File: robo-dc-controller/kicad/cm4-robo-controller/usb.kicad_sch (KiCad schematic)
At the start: 35 parts, among them U2 TPD4EUSB30DQAR-N, U3 FSUSB42MUX, U4 USB2514B-I/M2, U5 AP22653W6-7, U6 TPD4EUSB30DQAR-N, X1 X322524MOB4SI

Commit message: Fixing up usb.kicad+sch
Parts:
- removed C10, C6, C7, C8, C9: 100n, Capacitor_SMD:C_0402_1005Metric, symbol Device:C
- added C10, C19, C6, C7, C8, C9: 100nF, PCM_JLCPCB:C_0402, symbol PCM_JLCPCB-Capacitors:0402,100nF
- C3: VOLTAGE RATING (none) -> 10V
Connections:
- net 3V3_CM4: now also C10.1, C19.1, C6.1, C7.1, C8.1, C9.1
- net GND: now also C10.2, C19.2, C6.2, C7.2, C8.2, C9.2
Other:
- note added: "3.3V Caps for U3 and U4 VDD/VCC."
- note added: "4-Port USB Hub (only using 2 ports)"
- note added: "Current-limited high-side switch"
- note added: "Place each 100nF next to its own U4 supply pin (pins 5, 10, 15, 23, 29, 36) One 100nF place near pin 1 of U3"
- note added: "Ports 3 and 4 are unused: pins 6-9 aren't connected. Reset: RESET_N (pin 26) is on nEXTRST, which leaves this sheet."
- note added: "Protects both USB-A ports (4 lines). Diode clamps VBUS. Place both at USB1."
- note added: "Supplies and protects the 5V going out to the USB-A ports ILIM with 15K resistor limits to ~1.75A"
- note added: "USB - 2 Ports"
- note added: "USB-A ESD"
- note added: "USB-C ESD"
- note added: "USB-C Port for CM4 Flashing (rpiboot)"
- note added: "USB_OTG_ID: high = CM4 device mode (rpiboot), low/GND = CM4 host. Needs otg_mode=1 in config.txt."
- note removed: "U21 protects both USB-A ports (4 lines). D36 clamps VBUS. Place both at USB1."
- note removed: "USB"
- title: (none) -> USB
- moved on the sheet: C1, C11, C12, C13, C14, C15, C16, C2, C3, C4, C5, D1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

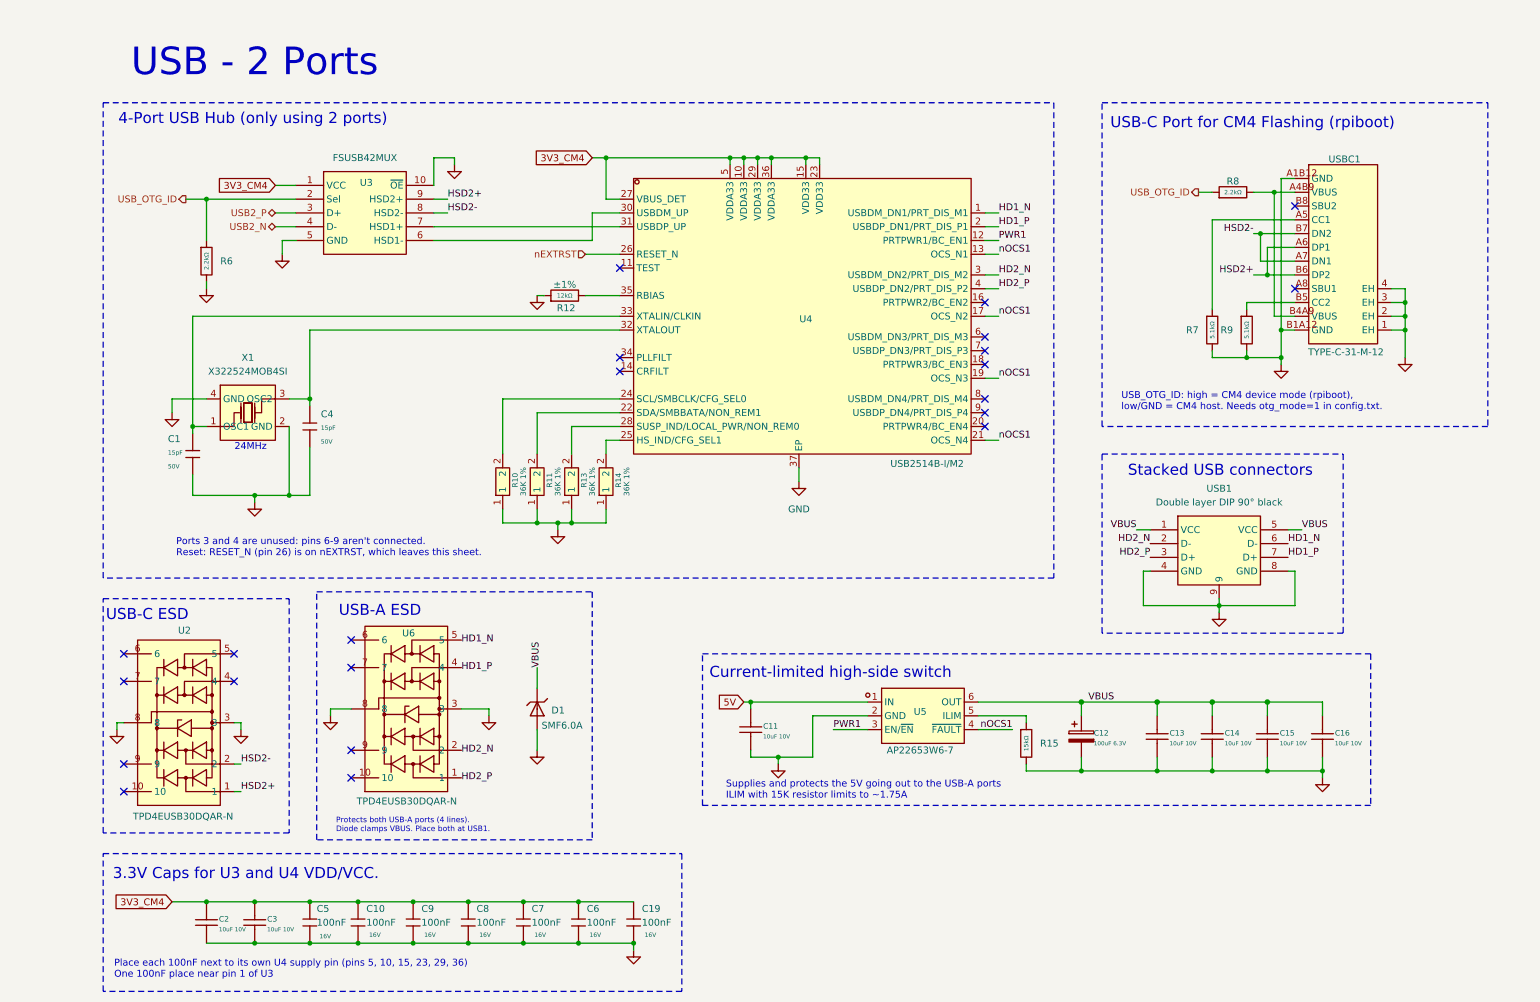
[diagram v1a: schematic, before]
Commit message: USB sheet: add 2-port expansion header, ESD, and design notes
Use all four USB2514B downstream ports: ports 1-2 stay on the USB1
type-A stack, ports 3-4 now go to J14, a 2x5 header with the standard
PC front-panel USB 2.0 pinout. Ports 3 and 4 were previously left
floating, which the Microchip design checklist disallows.

Add U11 (TPD4EUSB30) ESD protection on the expansion pair, D3 (SMF6.0A)
VBUS clamp and C20 local bulk at the header, plus C19 decoupling for
U3 VCC.

Move the 100nF decoupling caps to the JLC basic part (LCSC C1525) so
they are sourced in the assembly BOM, and set J14's pin types to
passive to clear the ERC warnings. ERC on this sheet is now clean.

Document the sheet: purpose of U2/U4/U5/U6, the USB-C device port and
its OTG signalling, the shared ~1.75A port-power budget, and the J14
key-pin assembly note.
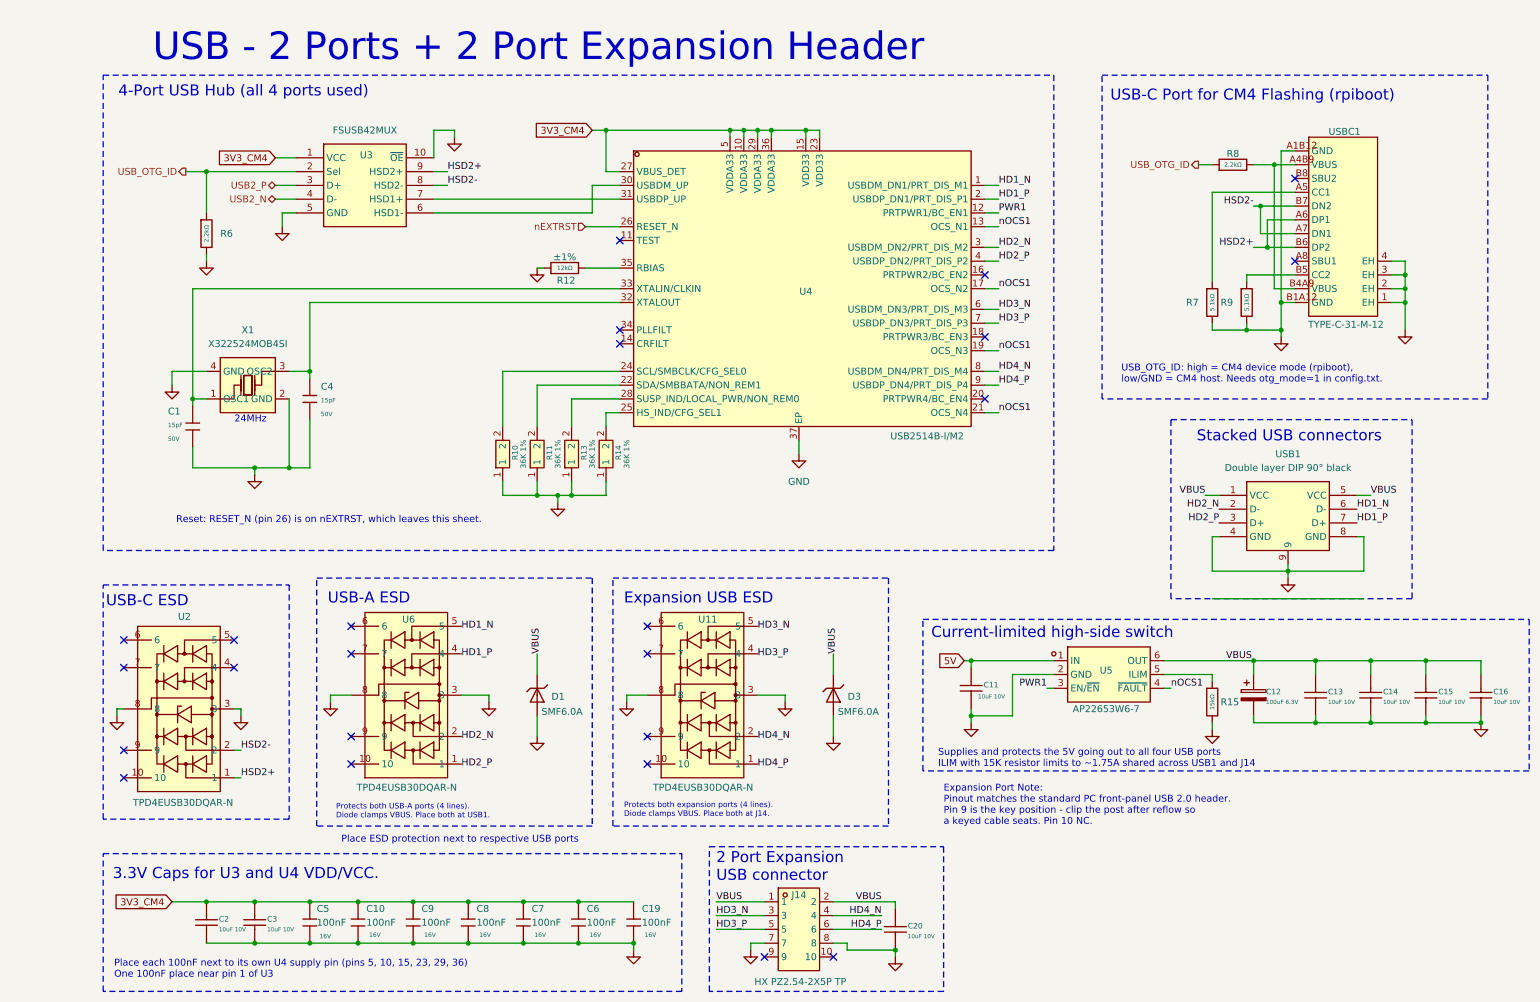
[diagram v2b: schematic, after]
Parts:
- added C20: 10uF 10V, MyParts:C0805, symbol MyParts:CL21B106KPQNNNE
- added D3: SMF6.0A, PCM_JLCPCB:D_SOD-123FL, symbol PCM_JLCPCB-Diodes:TVS-Uni,SMF6.0A
- added J14: HX PZ2.54-2X5P TP, MyParts:HDR-SMD_10P-P2.54-V-M-R2-C5-LS7.5, symbol MyParts:HXPZ2.54-2X5PTP
- added U11: TPD4EUSB30DQAR-N, MyParts:DFN-10_L2.5-W1.0-P0.50-BL-A, symbol MyParts:TPD4EUSB30DQAR-N
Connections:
- net GND: now also C20.1, D3.2, J14.7, J14.8, U11.3, U11.8
- net VBUS: now also C20.2, D3.1, J14.1, J14.2
- net HD3_N: now reaches U4.6 (USBDM_DN3/PRT_DIS_M3)
- net HD3_N: now also J14.3, U11.5
- net HD3_P: now reaches U4.7 (USBDP_DN3/PRT_DIS_P3)
- net HD3_P: now also J14.5, U11.4
- net HD4_N: now reaches U4.8 (USBDM_DN4/PRT_DIS_M4)
- net HD4_N: now also J14.4, U11.2
- net HD4_P: now reaches U4.9 (USBDP_DN4/PRT_DIS_P4)
- net HD4_P: now also J14.6, U11.1
- no-connect marks 22 -> 24
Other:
- note added: "2 Port Expansion USB connector"
- note added: "4-Port USB Hub (all 4 ports used)"
- note added: "Expansion Port Note: Pinout matches the standard PC front-panel USB 2.0 header. Pin 9 is the key position - clip the post after reflow so a keyed cable seats. Pin 10 NC."
- note added: "Expansion USB ESD"
- note added: "Place ESD protection next to respective USB ports"
- note added: "Protects both expansion ports (4 lines). Diode clamps VBUS. Place both at J14."
- note added: "Reset: RESET_N (pin 26) is on nEXTRST, which leaves this sheet."
- note added: "Supplies and protects the 5V going out to all four USB ports ILIM with 15K resistor limits to ~1.75A shared across USB1 and J14"
- note added: "USB - 2 Ports + 2 Port Expansion Header"
- note removed: "4-Port USB Hub (only using 2 ports)"
- note removed: "Ports 3 and 4 are unused: pins 6-9 aren't connected. Reset: RESET_N (pin 26) is on nEXTRST, which leaves this sheet."
- note removed: "Supplies and protects the 5V going out to the USB-A ports ILIM with 15K resistor limits to ~1.75A"
- note removed: "USB - 2 Ports"
- moved on the sheet: C1, C11, C12, C13, C14, C15, C16, C4, D1, R10, R11, R12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

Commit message: CM4 carrier: GPS sheet integration, U12 expansion header, power fixes
Populate U12 (2x12 expansion header) on the CM4_Connectors sheet:
all 19 CM4 signals plus 3V3_CM4 and four grounds, with 2.2k I2C
pull-ups (R113/R114) on GPIO2/GPIO3. Value matches the CM4IO
reference design, which uses 2.2k on SDA1/SCL1.

Wire the new GPS sheet (MAX-M10S) into the CM4 sheet: add sheet pins
for GPS_RX_MCU, GPS_TX_MCU and 1PPS_MCU. The UART lands on UART3
(GPIO4 = TXD3 to the GPS RXD, GPIO5 = RXD3 from the GPS TXD) and
1PPS on GPIO16. Needs dtoverlay=uart3 in config.txt. The leftover
CM4_TX/CM4_RX/1PPS_MCU hierarchical labels, which pointed at a root
sheet with no matching pins, become local labels on those nets.

Fix the orphaned 3V3 label on the GPS sheet, which left the MS621FE
backup cell with no charge path, and scope 3V3_CM4 to the CM4
hierarchy: local labels in the CM4 sheet, hierarchical labels plus
sheet pins in each consuming sub-sheet. Net membership is unchanged
at 30 nodes.

Add PWR_FLAGs on the 5V rail and on GND. Both are driven through
passive parts (an inductor and ground symbols respectively), so ERC
could not see a driver.

ERC: 55 -> 40 violations. Of the remainder, 30 are the RoboClaw U1,
which is placed on the root sheet but not yet wired.
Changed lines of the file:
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@@
 		)
 	)
-	(global_label "3V3_CM4"
+	(hierarchical_label "3V3_CM4"
 		(shape input)
 		(at 50.8 40.64 180)
-		(fields_autoplaced yes)
 		(effects
 			(font
@@
 			(justify right)
 		)
-		(property "Intersheetrefs" "${INTERSHEET_REFS}"
-			(at 39.4087 40.64 0)
-			(hide yes)
-			(show_name no)
-			(do_not_autoplace no)
-			(effects
-				(font
-					(size 1.27 1.27)
-				)
-				(justify right)
-			)
-		)
 	)
-	(global_label "3V3_CM4"
+	(hierarchical_label "3V3_CM4"
 		(shape input)
 		(at 109.22 35.56 180)
-		(fields_autoplaced yes)
 		(effects
 			(font
@@
 			(justify right)
 		)
-		(property "Intersheetrefs" "${INTERSHEET_REFS}"
-			(at 97.8287 35.56 0)
-			(hide yes)
-			(show_name no)
-			(do_not_autoplace no)
-			(effects
-				(font
-					(size 1.27 1.27)
-				)
-				(justify right)
-			)
-		)
 	)
 	(global_label "5V"
@@
 		)
 	)
-	(global_label "3V3_CM4"
+	(hierarchical_label "3V3_CM4"
 		(shape input)
 		(at 31.75 177.8 180)
-		(fields_autoplaced yes)
 		(effects
 			(font
@@
 			(justify right)
 		)
-		(property "Intersheetrefs" "${INTERSHEET_REFS}"
-			(at 20.3587 177.8 0)
-			(hide yes)
-			(show_name no)
-			(do_not_autoplace no)
-			(effects
-				(font
-					(size 1.27 1.27)
-				)
-				(justify right)
-			)
-		)
 	)
 	(hierarchical_label "USB2_N"
@@
 			)
 		)
-		(property "Description" ""
+		(property "Description" "Power symbol creates a global label with name \"GND\" , ground"
 			(at 165.1 187.96 0)
 			(show_name no)
@@
 			)
 		)
-		(property "Description" ""
+		(property "Description" "Power symbol creates a global label with name \"GND\" , ground"
 			(at 138.43 186.69 0)
 			(show_name no)

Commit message: Updates
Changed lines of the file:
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@@
 	(wire
 		(pts
-			(xy 223.52 121.92) (xy 251.46 121.92)
-		)
-		(stroke
-			(width 0)
-			(type default)
-		)
-	)
-	(wire
-		(pts
 			(xy 57.15 67.31) (xy 114.3 67.31)
 		)
@@
 		)
 	)
-	(hierarchical_label "3V3_CM4"
-		(shape input)
-		(at 50.8 40.64 180)
-		(effects
-			(font
-				(size 1.27 1.27)
-			)
-			(justify right)
-		)
-	)
-	(hierarchical_label "3V3_CM4"
-		(shape input)
-		(at 109.22 35.56 180)
-		(effects
-			(font
-				(size 1.27 1.27)
-			)
-			(justify right)
-		)
-	)
 	(global_label "5V"
 		(shape input)
@@
 		)
 	)
-	(hierarchical_label "3V3_CM4"
-		(shape input)
-		(at 31.75 177.8 180)
-		(effects
-			(font
-				(size 1.27 1.27)
-			)
-			(justify right)
-		)
-	)
 	(hierarchical_label "USB2_N"
 		(shape bidirectional)
@@
 		)
 	)
+	(hierarchical_label "3V3_CM4"
+		(shape input)
+		(at 50.8 40.64 180)
+		(effects
+			(font
+				(size 1.27 1.27)
+			)
+			(justify right)
+		)
+	)
+	(hierarchical_label "3V3_CM4"
+		(shape input)
+		(at 109.22 35.56 180)
+		(effects
+			(font
+				(size 1.27 1.27)
+			)
+			(justify right)
+		)
+	)
 	(hierarchical_label "USB2_P"
 		(shape bidirectional)
@@
 		)
 	)
+	(hierarchical_label "3V3_CM4"
+		(shape input)
+		(at 31.75 177.8 180)
+		(effects
+			(font
+				(size 1.27 1.27)
+			)
+			(justify right)
+		)
+	)
 	(hierarchical_label "nEXTRST"
 		(shape input)
@@
 		(property "Description" "Power symbol creates a global label with name \"GND\" , ground"
 			(at 165.1 187.96 0)
+			(hide yes)
 			(show_name no)
 			(do_not_autoplace no)
@@
 		(property "Description" "Power symbol creates a global label with name \"GND\" , ground"
 			(at 138.43 186.69 0)
+			(hide yes)
 			(show_name no)
 			(do_not_autoplace no)
